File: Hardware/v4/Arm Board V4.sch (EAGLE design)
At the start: 57 parts, among them IC3 L6206D, U1 SN74LS241DW, U2 XBEE-1B3, U3 LSM9DS0

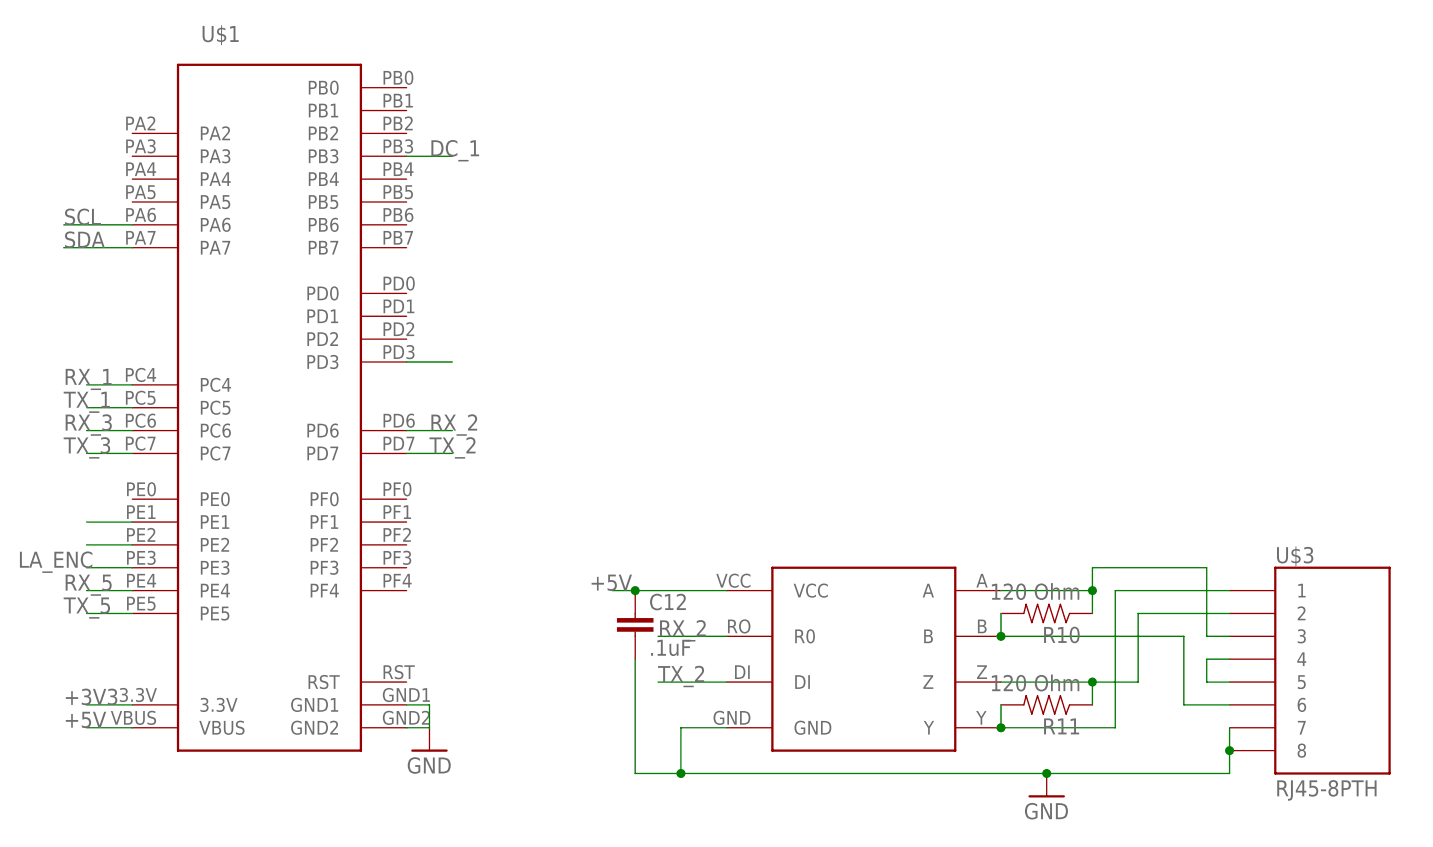
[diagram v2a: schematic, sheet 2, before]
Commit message: Positioned all the caps correctly
I think the board is finished but may change as I look for parts to make
sure everything is correct
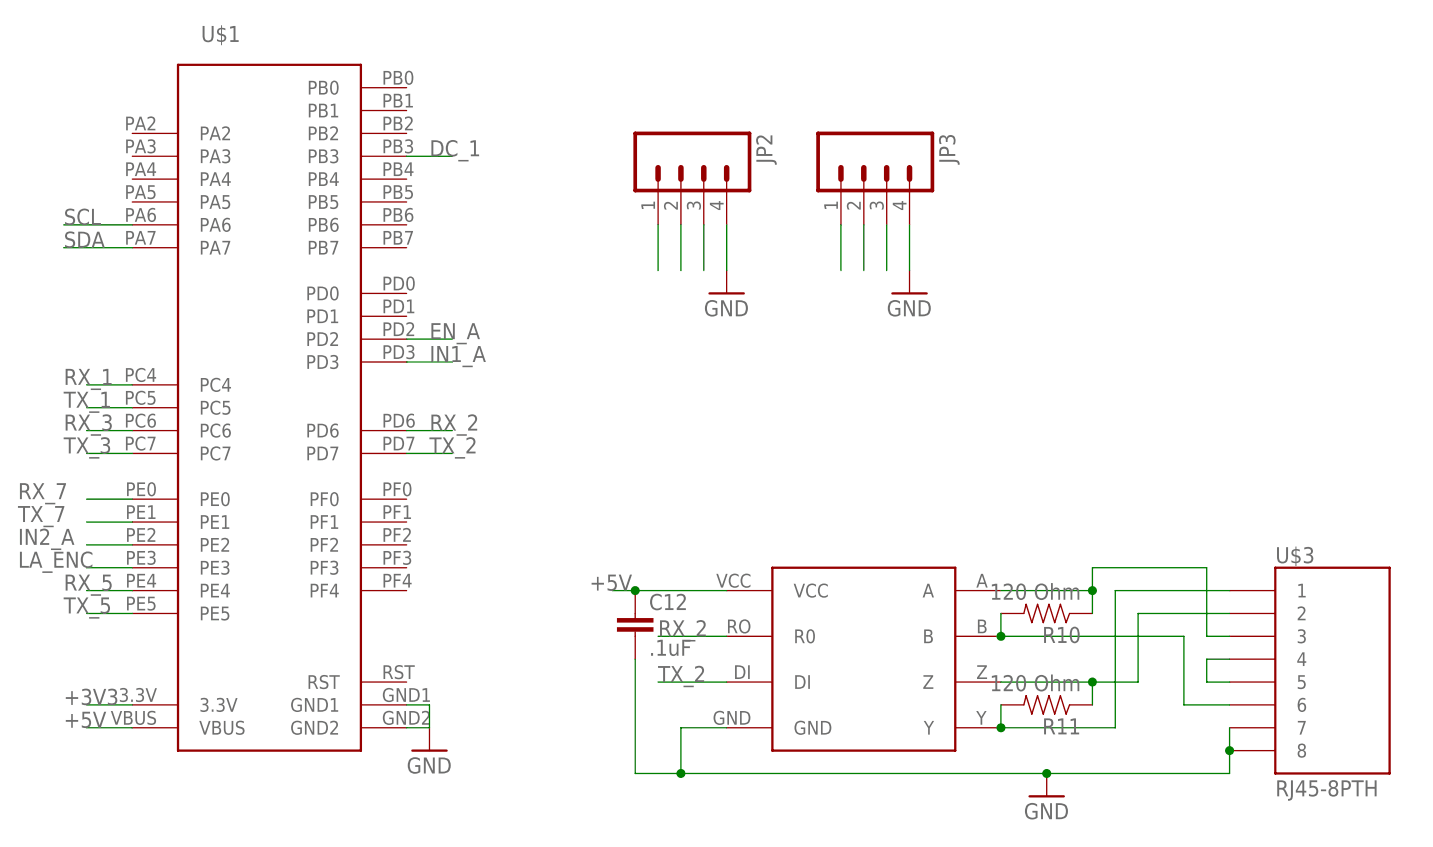
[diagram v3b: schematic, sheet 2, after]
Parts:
- added JP2, JP3: (no value), SparkFun-Connectors:M04PTH
- JP1: device SparkFun-Connectors:M04POLAR -> SparkFun-Connectors:M04PTH
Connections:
- new net RX_7: JP2.2, U$1.PE0
- new net TX_7: JP2.1, U$1.PE1
- net +5V: now also JP2.3, JP3.3
- net EN_A: now also U$1.PD2; no longer U$1.PD3
- net GND: now also JP2.4, JP3.4
- net IN1_A: now also U$1.PD3; no longer U$1.PE1
- net RX_5: now also JP3.2
- net TX_5: now also JP3.1
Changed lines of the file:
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@@
 <?xml version="1.0" encoding="utf-8"?>
 <!DOCTYPE eagle SYSTEM "eagle.dtd">
-<eagle version="7.1.0">
+<eagle version="6.5.0">
 <drawing>
 <settings>
@@
 <part name="C9" library="SparkFun-Passives" deviceset="CAP" device="1206" value="10nF"/>
 <part name="R15" library="SparkFun-Resistors" deviceset="RESISTOR" device="1206" value="100"/>
-<part name="JP1" library="SparkFun-Connectors" deviceset="M04" device="POLAR"/>
+<part name="JP1" library="SparkFun-Connectors" deviceset="M04" device="PTH"/>
 <part name="GND6" library="SparkFun-Aesthetics" deviceset="GND" device=""/>
 <part name="C10" library="SparkFun-Capacitors" deviceset="CAP_POL" device="E" value="330uF"/>
@@
 <part name="C15" library="SparkFun-Capacitors" deviceset="1.0UF50V10%(1206)" device="" value="1.0uF"/>
 <part name="GND32" library="SparkFun-Aesthetics" deviceset="GND" device=""/>
+<part name="JP2" library="SparkFun-Connectors" deviceset="M04" device="PTH"/>
+<part name="JP3" library="SparkFun-Connectors" deviceset="M04" device="PTH"/>
+<part name="GND33" library="supply1" deviceset="GND" device=""/>
+<part name="GND34" library="supply1" deviceset="GND" device=""/>
 </parts>
 <sheets>
@@
 <instance part="GND8" gate="1" x="43.18" y="5.08"/>
 <instance part="U$4" gate="G$1" x="91.44" y="15.24"/>
+<instance part="JP2" gate="G$1" x="71.12" y="68.58" rot="R270"/>
+<instance part="JP3" gate="G$1" x="91.44" y="68.58" rot="R270"/>
+<instance part="GND33" gate="1" x="96.52" y="55.88"/>
+<instance part="GND34" gate="1" x="76.2" y="55.88"/>
 </instances>
 <busses>
@@
 <wire x1="40.64" y1="7.62" x2="43.18" y2="7.62" width="0.1524" layer="91"/>
 </segment>
+<segment>
+<pinref part="JP3" gate="G$1" pin="4"/>
+<pinref part="GND33" gate="1" pin="GND"/>
+<wire x1="96.52" y1="58.42" x2="96.52" y2="63.5" width="0.1524" layer="91"/>
+</segment>
+<segment>
+<pinref part="JP2" gate="G$1" pin="4"/>
+<pinref part="GND34" gate="1" pin="GND"/>
+<wire x1="76.2" y1="58.42" x2="76.2" y2="63.5" width="0.1524" layer="91"/>
+</segment>
 </net>
 <net name="N$5" class="0">
@@
 <label x="2.54" y="22.86" size="1.778" layer="95"/>
 </segment>
+<segment>
+<pinref part="JP3" gate="G$1" pin="2"/>
+<wire x1="91.44" y1="63.5" x2="91.44" y2="58.42" width="0.1524" layer="91"/>
+</segment>
 </net>
 <net name="TX_5" class="0">
@@
 <wire x1="10.16" y1="20.32" x2="5.08" y2="20.32" width="0.1524" layer="91"/>
 <label x="2.54" y="20.32" size="1.778" layer="95"/>
+</segment>
+<segment>
+<pinref part="JP3" gate="G$1" pin="1"/>
+<wire x1="88.9" y1="63.5" x2="88.9" y2="58.42" width="0.1524" layer="91"/>
 </segment>
 </net>
@@
 <wire x1="129.54" y1="12.7" x2="132.08" y2="12.7" width="0.1524" layer="91"/>
 </segment>
+<segment>
+<pinref part="JP2" gate="G$1" pin="3"/>
+<wire x1="73.66" y1="63.5" x2="73.66" y2="58.42" width="0.1524" layer="91"/>
+</segment>
+<segment>
+<pinref part="JP3" gate="G$1" pin="3"/>
+<wire x1="93.98" y1="63.5" x2="93.98" y2="58.42" width="0.1524" layer="91"/>
+</segment>
 </net>
 <net name="LA_ENC" class="0">
@@
 </segment>
 </net>
-<net name="IN1_A" class="0">
+<net name="EN_A" class="0">
+<segment>
+<pinref part="U$1" gate="G$1" pin="PD2"/>
+<wire x1="40.64" y1="50.8" x2="45.72" y2="50.8" width="0.1524" layer="91"/>
+<label x="43.18" y="50.8" size="1.778" layer="95"/>
+</segment>
+</net>
+<net name="IN2_A" class="0">
+<segment>
+<pinref part="U$1" gate="G$1" pin="PE2"/>
+<wire x1="10.16" y1="27.94" x2="5.08" y2="27.94" width="0.1524" layer="91"/>
+<label x="-2.54" y="27.94" size="1.778" layer="95"/>
+</segment>
+</net>
+<net name="RX_7" class="0">
+<segment>
+<pinref part="U$1" gate="G$1" pin="PE0"/>
+<wire x1="10.16" y1="33.02" x2="5.08" y2="33.02" width="0.1524" layer="91"/>
+<label x="-2.54" y="33.02" size="1.778" layer="95"/>
+</segment>
+<segment>
+<pinref part="JP2" gate="G$1" pin="2"/>
+<wire x1="71.12" y1="63.5" x2="71.12" y2="58.42" width="0.1524" layer="91"/>
+</segment>
+</net>
+<net name="TX_7" class="0">
 <segment>
 <pinref part="U$1" gate="G$1" pin="PE1"/>
 <wire x1="10.16" y1="30.48" x2="5.08" y2="30.48" width="0.1524" layer="91"/>
-</segment>
-</net>
-<net name="EN_A" class="0">
+<label x="-2.54" y="30.48" size="1.778" layer="95"/>
+</segment>
+<segment>
+<pinref part="JP2" gate="G$1" pin="1"/>
+<wire x1="68.58" y1="63.5" x2="68.58" y2="58.42" width="0.1524" layer="91"/>
+</segment>
+</net>
+<net name="IN1_A" class="0">
 <segment>
 <pinref part="U$1" gate="G$1" pin="PD3"/>
 <wire x1="40.64" y1="48.26" x2="45.72" y2="48.26" width="0.1524" layer="91"/>
-</segment>
-</net>
-<net name="IN2_A" class="0">
-<segment>
-<pinref part="U$1" gate="G$1" pin="PE2"/>
-<wire x1="10.16" y1="27.94" x2="5.08" y2="27.94" width="0.1524" layer="91"/>
-</segment>
-</net>
+<label x="43.18" y="48.26" size="1.778" layer="95"/>
+</segment>
+</net>

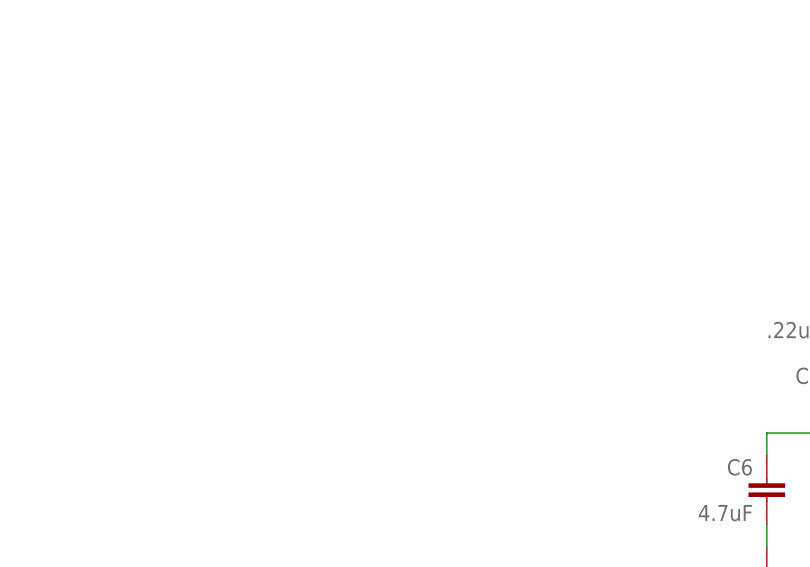
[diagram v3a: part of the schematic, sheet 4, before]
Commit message: Added headers for IMU breakout
In addition to keeping the IMU chip on the board.
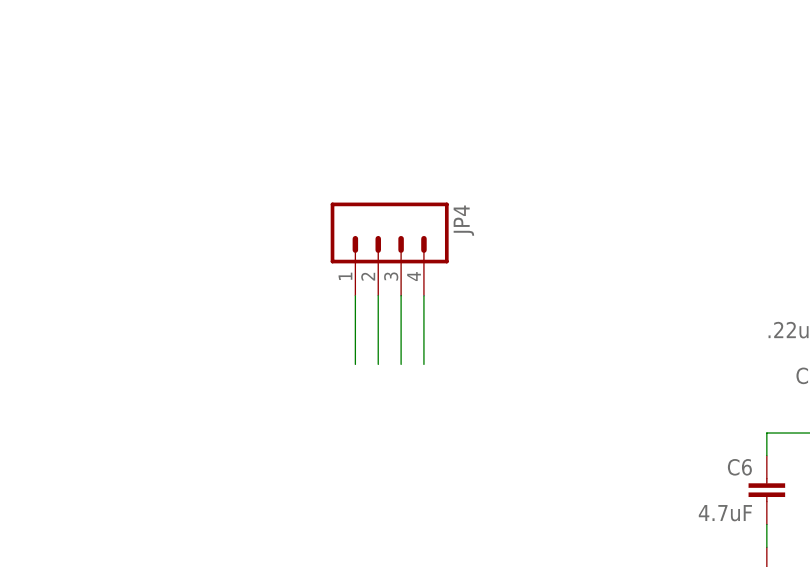
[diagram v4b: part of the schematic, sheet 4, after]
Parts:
- added JP4: (no value), SparkFun-Connectors:M04PTH
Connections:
- net +3V3: now also JP4.2
- net GND: now also JP4.1
- net SCL: now also JP4.4
- net SDA: now also JP4.3
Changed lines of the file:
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@@
 <?xml version="1.0" encoding="utf-8"?>
 <!DOCTYPE eagle SYSTEM "eagle.dtd">
-<eagle version="6.5.0">
+<eagle version="7.1.0">
 <drawing>
 <settings>
@@
 <part name="GND33" library="supply1" deviceset="GND" device=""/>
 <part name="GND34" library="supply1" deviceset="GND" device=""/>
+<part name="JP4" library="SparkFun-Connectors" deviceset="M04" device="PTH"/>
 </parts>
 <sheets>
@@
 <instance part="R6" gate="G$1" x="17.78" y="33.02" rot="R90"/>
 <instance part="R7" gate="G$1" x="33.02" y="33.02" rot="R90"/>
+<instance part="JP4" gate="G$1" x="53.34" y="121.92" rot="R270"/>
 </instances>
 <busses>
@@
 <wire x1="127" y1="134.62" x2="127" y2="137.16" width="0.1524" layer="91"/>
 </segment>
+<segment>
+<pinref part="JP4" gate="G$1" pin="1"/>
+<wire x1="50.8" y1="116.84" x2="50.8" y2="109.22" width="0.1524" layer="91"/>
+</segment>
 </net>
 <net name="SDA" class="0">
@@
 <label x="101.6" y="25.4" size="1.27" layer="95" rot="R180" xref="yes"/>
 </segment>
+<segment>
+<pinref part="JP4" gate="G$1" pin="3"/>
+<wire x1="55.88" y1="116.84" x2="55.88" y2="109.22" width="0.1524" layer="91"/>
+</segment>
 </net>
 <net name="SCL" class="0">
@@
 <wire x1="116.84" y1="25.4" x2="119.38" y2="25.4" width="0.1524" layer="91"/>
 <label x="116.84" y="25.4" size="1.27" layer="95" rot="R180" xref="yes"/>
+</segment>
+<segment>
+<pinref part="JP4" gate="G$1" pin="4"/>
+<wire x1="58.42" y1="116.84" x2="58.42" y2="109.22" width="0.1524" layer="91"/>
 </segment>
 </net>
@@
 <label x="104.14" y="129.54" size="1.778" layer="95"/>
 </segment>
-</net>
+<segment>
+<pinref part="JP4" gate="G$1" pin="2"/>
+<wire x1="53.34" y1="116.84" x2="53.34" y2="109.22" width="0.1524" layer="91"/>
+</segment>
+</net>

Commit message: Start of changes for Nathan
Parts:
- removed C15: 1.0uF, SparkFun-Capacitors:1.0UF50V10%(1206)
- added C23: 4.7uF, SparkFun-Capacitors:CAP1206
- C11: value 4.7uF -> 1.0uF; device SparkFun-Capacitors:CAP1206 -> SparkFun-Capacitors:1.0UF50V10%(1206)
- renumbered C1 to C21, C13 to C24, C14 to C20, C3 to C22, C5 to C39, C6 to C38, C7 to C37, C8 to C36, R2 to R35, R3 to R34, R4 to R30, R5 to R31, R6 to R33, R7 to R32, U$1 to P1
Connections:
- net 14.8V: now also C11.1; no longer C15.1
- net GND: now also C23.2; no longer C15.2
- net VIN: now also C23.1; no longer C11.1

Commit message: Finished Version 4 of the board
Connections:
- net INT1_XM: now also P1.PB1
- net INT2_XM: now also P1.PB0
- net INT_G: now also P1.PB5
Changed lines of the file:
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@@
 <?xml version="1.0" encoding="utf-8"?>
 <!DOCTYPE eagle SYSTEM "eagle.dtd">
-<eagle version="7.1.0">
+<eagle version="6.5.0">
 <drawing>
 <settings>
@@
 </segment>
 </net>
+<net name="INT_G" class="0">
+<segment>
+<pinref part="P1" gate="G$1" pin="PB5"/>
+<wire x1="40.64" y1="66.04" x2="48.26" y2="66.04" width="0.1524" layer="91"/>
+</segment>
+</net>
+<net name="INT1_XM" class="0">
+<segment>
+<pinref part="P1" gate="G$1" pin="PB1"/>
+<wire x1="40.64" y1="76.2" x2="48.26" y2="76.2" width="0.1524" layer="91"/>
+</segment>
+</net>
+<net name="INT2_XM" class="0">
+<segment>
+<pinref part="P1" gate="G$1" pin="PB0"/>
+<wire x1="40.64" y1="78.74" x2="48.26" y2="78.74" width="0.1524" layer="91"/>
+</segment>
+</net>
